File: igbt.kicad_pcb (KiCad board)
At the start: 2 copper layers, 45 parts, among them J1 PWM, J10 Motor, J2 V_Gate, J7 Sense_AC_B, J8 Sense_AC_A, J9 DC_Sense, Q1 IRG4PF50W, Q2 IRG4PF50W, Q3 IRG4PF50W, Q4 IRG4PF50W, Q5 IRG4PF50W, Q6 IRG4PF50W, U1 ACS758xCB-050B-PFF, U2 ACS758xCB-050B-PFF, U5 IR2110, U6 IR2110, U7 IR2110

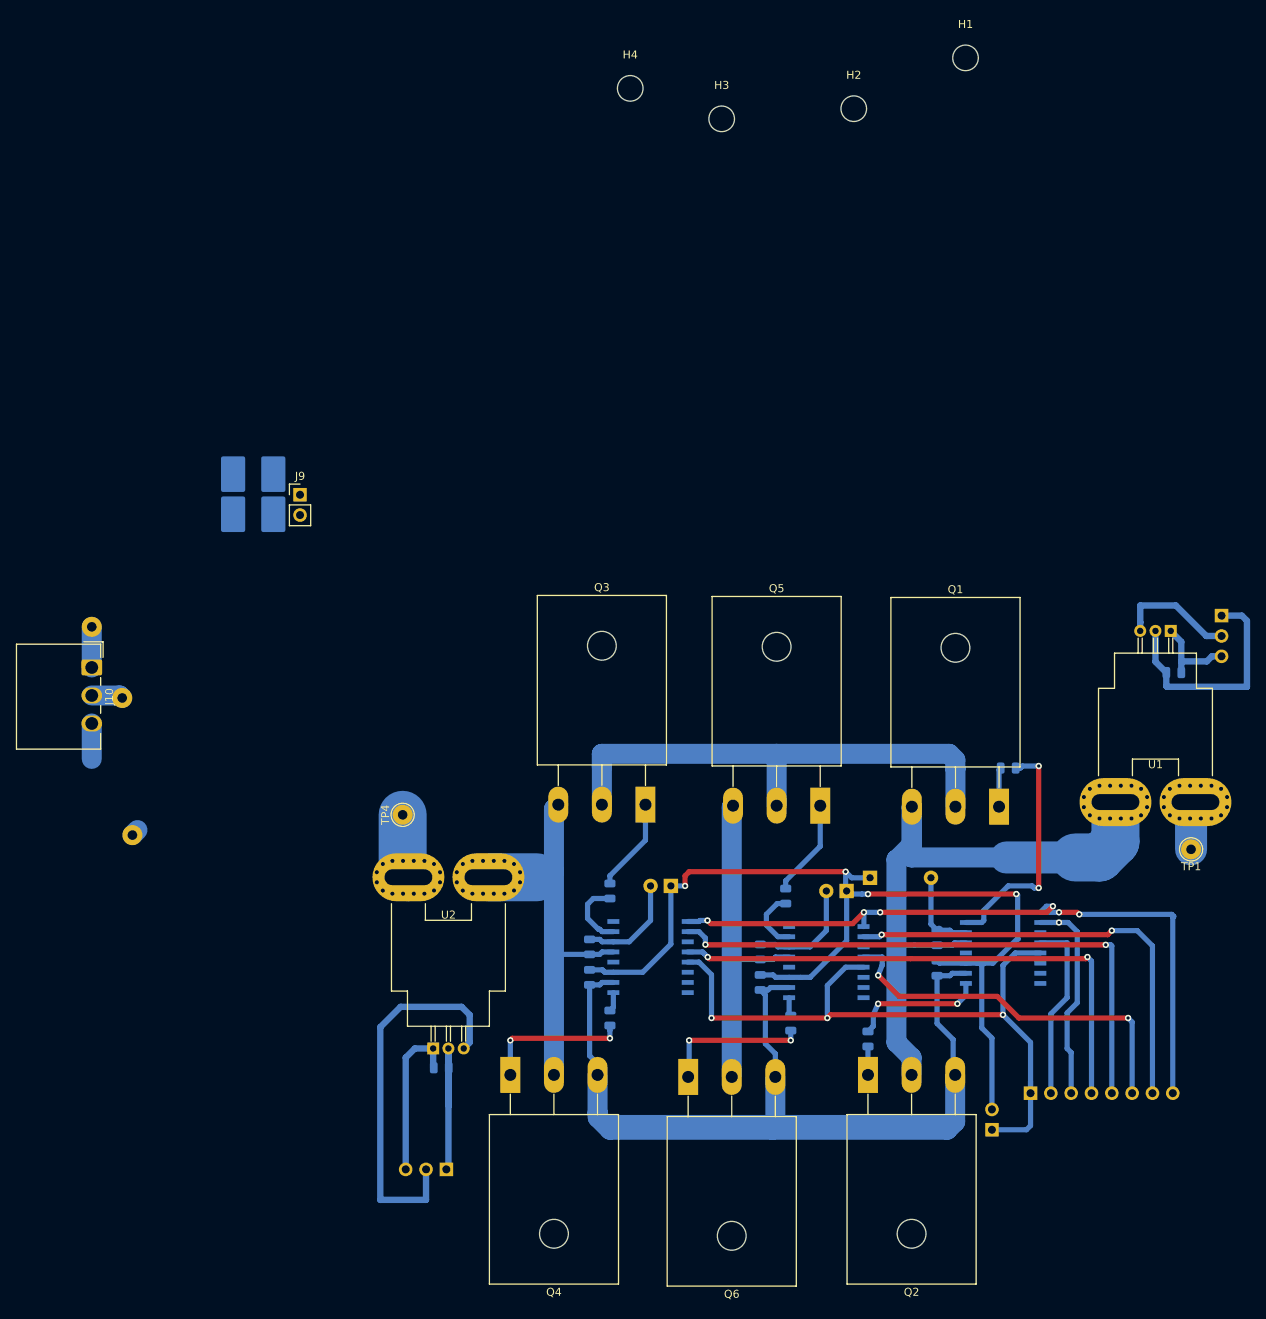
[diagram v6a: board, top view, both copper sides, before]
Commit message: enlarged vias
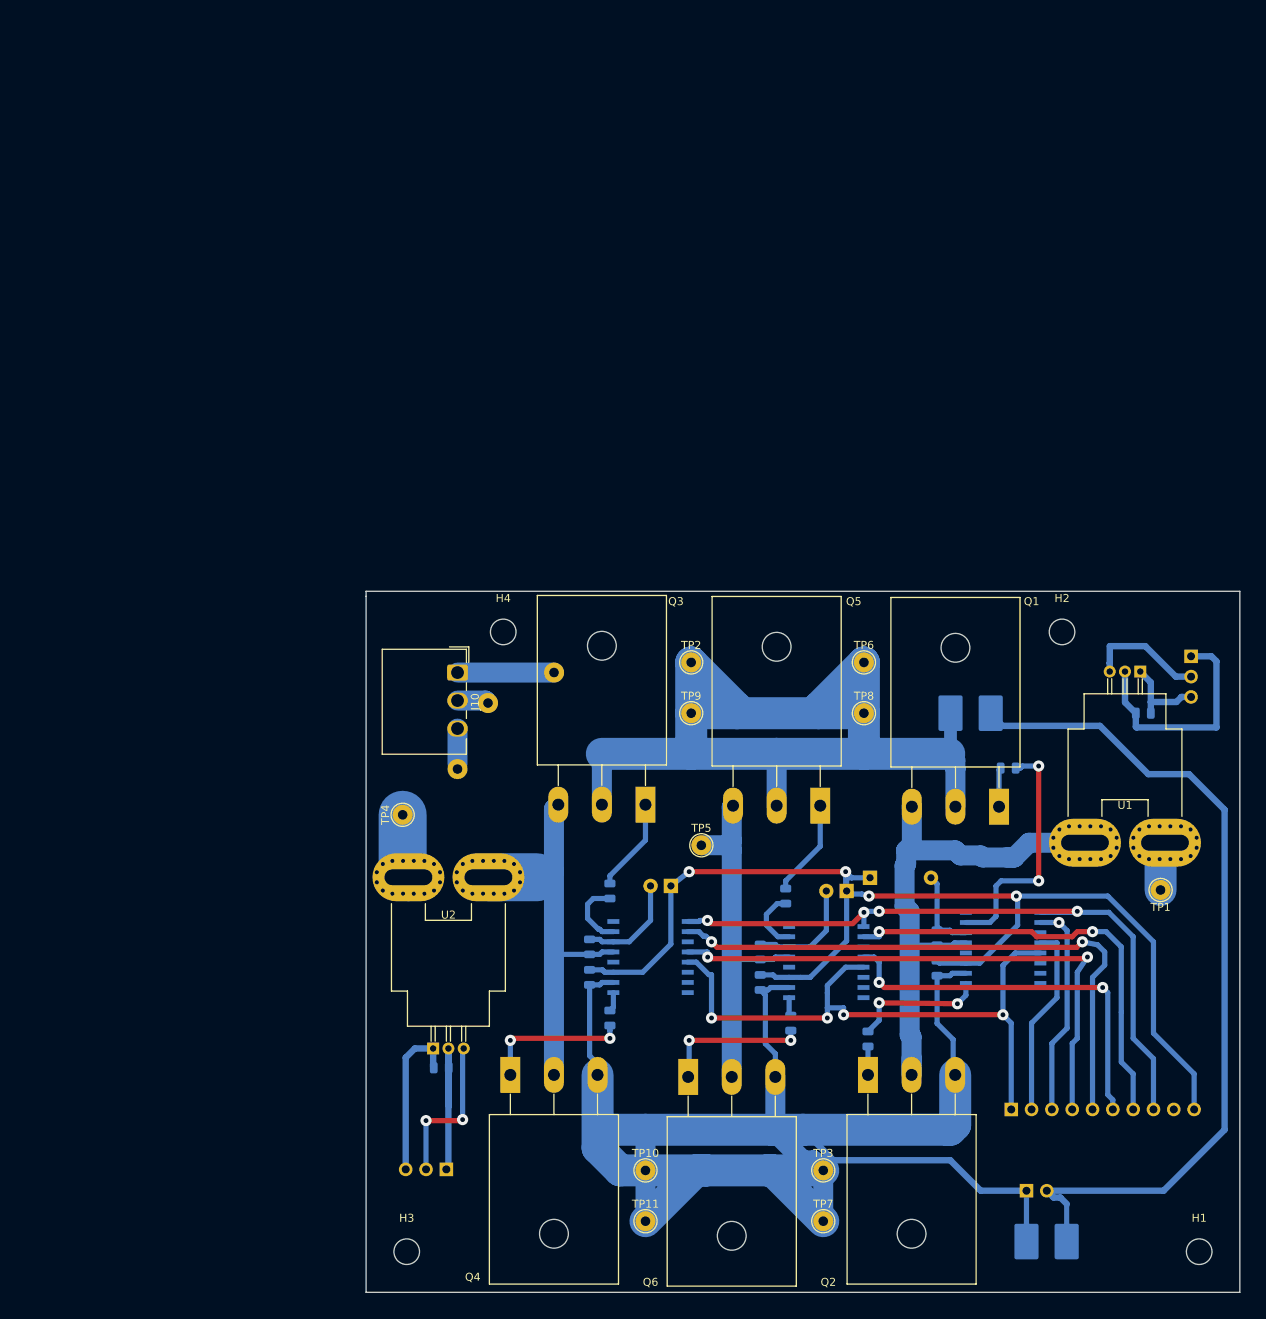
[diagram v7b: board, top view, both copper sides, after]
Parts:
- removed J2: V_Gate, Connector_PinHeader_2.54mm:PinHeader_1x02_P2.54mm_Vertical
- added TP10: DC_CapB_N, TestPoint:TestPoint_THTPad_D2.5mm_Drill1.2mm, F.Cu at (98.4, 127.0)
- added TP11: DC_CapC_N, TestPoint:TestPoint_THTPad_D2.5mm_Drill1.2mm, F.Cu at (98.4, 133.3)
- added TP2: DC_CapB_P, TestPoint:TestPoint_THTPad_D2.5mm_Drill1.2mm, F.Cu at (104.1, 63.5)
- added TP3: DC_CapA_N, TestPoint:TestPoint_THTPad_D2.5mm_Drill1.2mm, F.Cu at (120.7, 127.0)
- added TP5: C, TestPoint:TestPoint_THTPad_D2.5mm_Drill1.2mm, F.Cu at (105.4, 86.4)
- added TP6: DC_BUS, TestPoint:TestPoint_THTPad_D2.5mm_Drill1.2mm, F.Cu at (125.7, 63.5)
- added TP7: DC_GND, TestPoint:TestPoint_THTPad_D2.5mm_Drill1.2mm, F.Cu at (120.7, 133.3)
- added TP8: DC_CapA_P, TestPoint:TestPoint_THTPad_D2.5mm_Drill1.2mm, F.Cu at (125.7, 69.8)
- added TP9: DC_CapC_P, TestPoint:TestPoint_THTPad_D2.5mm_Drill1.2mm, F.Cu at (104.1, 69.8)
- J1: footprint Connector_PinHeader_2.54mm:PinHeader_1x08_P2.54mm_Vertical -> Connector_PinHeader_2.54mm:PinHeader_1x10_P2.54mm_Vertical
- J9: moved to B.Cu
- moved H1 152.1 mm to (167.6, 137.2)
- moved H3 147.0 mm to (68.6, 137.2)
- moved R32 134.5 mm to (148.6, 135.9)
- moved J9 125.8 mm to (146.1, 129.5), turned to 270 degrees
- moved R8 94.5 mm to (139.1, 69.8), turned to 180 degrees
- moved H2 70.4 mm to (150.5, 59.7)
- moved H4 69.8 mm to (80.6, 59.7)
- moved TP12 58.1 mm to (87.0, 64.8)
- moved J10 45.7 mm to (74.9, 64.8)
- moved TP13 45.7 mm to (78.7, 68.6)
- moved TP14 41.5 mm to (74.9, 76.8)
- moved C4 6.35 mm to (160.7, 69.8)
- moved J8 6.35 mm to (166.6, 62.7)
- moved TP1 6.35 mm to (162.8, 91.9)
- moved U1 6.35 mm to (160.3, 64.6)
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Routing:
- net /bus_sense: track 0.00 -> 107.5 mm
- net Net-(Q1-Pad2): track 63.2 -> 153.1 mm
- net /DC_Link_GND: track 168.0 -> 247.7 mm
- net Net-(J7-Pad2): track 48.3 -> 19.7 mm, vias 0 -> 2
- net Net-(C2-Pad1): track 124.7 -> 148.7 mm
- net Net-(C1-Pad2): track 82.0 -> 67.9 mm
- net Net-(J1-Pad1): track 88.5 -> 79.6 mm, vias 3 -> 4
- net Net-(J10-Pad1): track 5.08 -> 12.1 mm
- net Net-(C7-Pad2): track 75.2 -> 79.3 mm
- net /B_L: track 67.6 -> 70.4 mm
- net Net-(J1-Pad8): track 89.5 -> 87.1 mm, vias 6 -> 4
- net /B_H: track 72.6 -> 73.9 mm
- net /A_L: track 23.0 -> 24.2 mm
- net /C_L: track 47.8 -> 48.7 mm
- net Net-(J10-Pad3): track 5.33 -> 4.43 mm
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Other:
- board outline added: 109.2 x 87.6 mm
- board text added: "A"
- board text added: "B"
- board text added: "C"

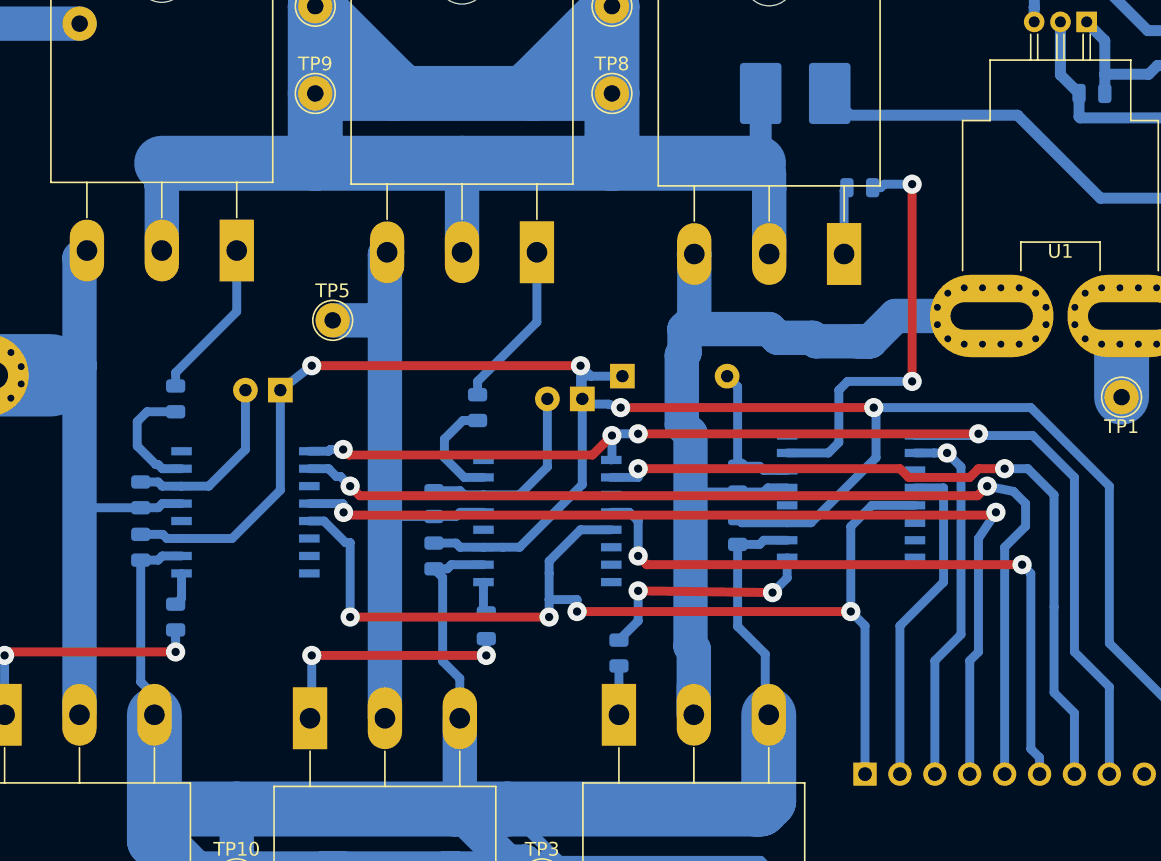
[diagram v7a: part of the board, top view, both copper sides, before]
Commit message: IR2110 changed to IR2110S
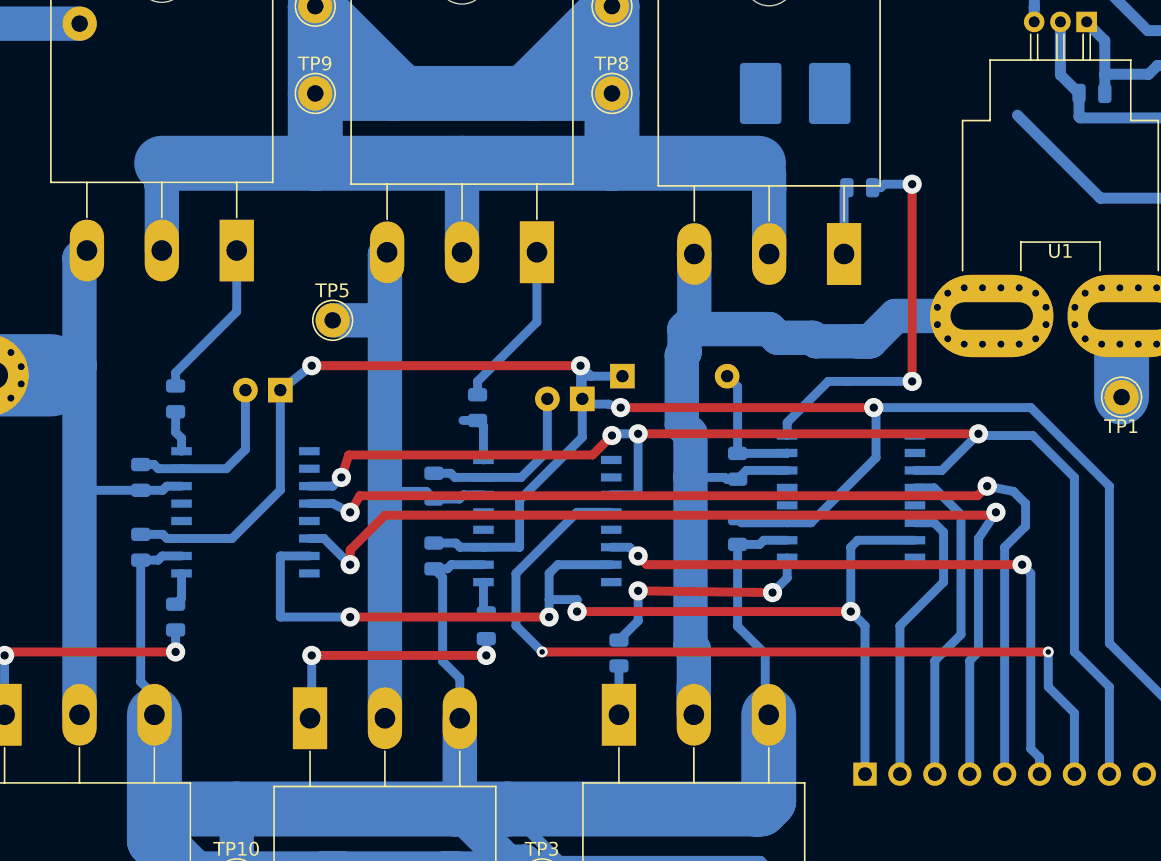
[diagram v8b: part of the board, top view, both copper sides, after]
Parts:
- moved C3 1.27 mm to (91.4, 97.8)
- moved C7 1.27 mm to (112.8, 98.4)
- moved C1 0.94 mm to (134.9, 97.0)
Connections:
- R8 pad 1: /bus_sense -> (no net)
- R8 pad 2: Net-(Q1-Pad2) -> (no net)
- U5 pad 10: /A_H -> (no net)
- U5 pad 11: (no net) -> Net-(J1-Pad8)
- U5 pad 12: /A_L -> /A_H
- U5 pad 13: Net-(J1-Pad1) -> (no net)
- U5 pad 14: (no net) -> /A_L
- U5 pad 15: (no net) -> Net-(J1-Pad1)
- U5 pad 5: Net-(C1-Pad2) -> (no net)
- U5 pad 6: Net-(C1-Pad1) -> Net-(C1-Pad2)
- U5 pad 7: Net-(R11-Pad2) -> Net-(C1-Pad1)
- U5 pad 8: (no net) -> Net-(R11-Pad2)
- U5 pad 9: Net-(J1-Pad8) -> (no net)
- U6 pad 10: /B_H -> (no net)
- U6 pad 11: (no net) -> Net-(J1-Pad8)
- U6 pad 12: /B_L -> /B_H
- U6 pad 13: Net-(J1-Pad1) -> (no net)
- U6 pad 14: (no net) -> /B_L
- U6 pad 15: (no net) -> Net-(J1-Pad1)
- U6 pad 5: Net-(C3-Pad2) -> (no net)
- U6 pad 6: Net-(C3-Pad1) -> Net-(C3-Pad2)
- U6 pad 7: Net-(R2-Pad2) -> Net-(C3-Pad1)
- U6 pad 8: (no net) -> Net-(R2-Pad2)
- U6 pad 9: Net-(J1-Pad8) -> (no net)
- U7 pad 10: /C_H -> (no net)
- U7 pad 11: (no net) -> Net-(J1-Pad8)
- U7 pad 12: /C_L -> /C_H
- U7 pad 13: Net-(J1-Pad1) -> (no net)
- U7 pad 14: (no net) -> /C_L
- U7 pad 15: (no net) -> Net-(J1-Pad1)
- U7 pad 5: Net-(C7-Pad2) -> (no net)
- U7 pad 6: Net-(C7-Pad1) -> Net-(C7-Pad2)
- U7 pad 7: Net-(R17-Pad2) -> Net-(C7-Pad1)
- U7 pad 8: (no net) -> Net-(R17-Pad2)
- U7 pad 9: Net-(J1-Pad8) -> (no net)
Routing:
- net /bus_sense: track 107.5 -> 93.2 mm
- net Net-(J1-Pad8): track 87.1 -> 94.0 mm
- net /C_H: track 55.1 -> 61.8 mm
- net Net-(R2-Pad2): track 8.78 -> 3.05 mm
- net Net-(Q1-Pad2): track 153.1 -> 148.2 mm
- net Net-(R17-Pad2): track 7.76 -> 4.12 mm
- net /A_H: track 26.9 -> 23.8 mm, vias 1 -> 0
- net /A_L: track 24.2 -> 21.3 mm
- net /C_L: track 48.7 -> 46.2 mm
- net /B_L: track 70.4 -> 72.6 mm
- net Net-(R11-Pad2): track 30.8 -> 28.6 mm
- net Net-(C1-Pad1): track 11.0 -> 9.55 mm
- net Net-(C7-Pad1): track 14.2 -> 13.0 mm
- net Net-(J1-Pad1): track 79.6 -> 78.7 mm
- net Net-(C1-Pad2): track 67.9 -> 68.7 mm
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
